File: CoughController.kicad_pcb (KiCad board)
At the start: 2 copper layers, 144 x 100 mm, 59 parts, among them J1 カフＳＷ１, J10 音声入力, J11 音声出力, J12 DI-2, J13 DO-2, J14 CD1/CD2, J15 CF/MD, J16 IN1/IN2, J17 IN3/IN4, J2 カフＳＷ２, J3 カフＳＷ３, J4 カフＳＷ４, J5 カフＳＷ５, J6 電源入力, J7 電源出力, J8 DI-1, J9 DO-1, K1 G6A-274P-ST-US DC12, K2 G6A-274P-ST-US DC12, U1 TLP627-2, U2 TLP627-2, U3 TLP627-2, U4 TLP627-2, U5 TLP627-2, U6 TLP627-2, U7 TLP627-2, U8 TLP627-2

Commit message: カフコントローラ
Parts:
- added J18: Out, Connector_PinHeader_2.54mm:PinHeader_1x02_P2.54mm_Vertical, F.Cu at (79.3, 55.0)
- added J19: In, Connector_PinHeader_2.54mm:PinHeader_1x03_P2.54mm_Vertical, F.Cu at (69.6, 55.0)
- J1: value カフＳＷ１ -> SW1; footprint Connector_PinHeader_1.27mm:PinHeader_1x04_P1.27mm_Vertical -> Connector_PinHeader_2.54mm:PinHeader_1x04_P2.54mm_Vertical
- J10: value 音声入力 -> AUDIO_IN; footprint Connector_PinHeader_1.27mm:PinHeader_1x06_P1.27mm_Vertical -> Connector_PinHeader_2.54mm:PinHeader_1x06_P2.54mm_Vertical
- J11: value 音声出力 -> AUDIO_OUT; footprint Connector_PinHeader_1.27mm:PinHeader_1x06_P1.27mm_Vertical -> Connector_PinHeader_2.54mm:PinHeader_1x06_P2.54mm_Vertical
- J14, J15, J16, J17: footprint Connector_PinHeader_1.27mm:PinHeader_1x09_P1.27mm_Vertical -> Connector_PinHeader_2.54mm:PinHeader_1x09_P2.54mm_Vertical
- J2: value カフＳＷ２ -> SW2; footprint Connector_PinHeader_1.27mm:PinHeader_1x04_P1.27mm_Vertical -> Connector_PinHeader_2.54mm:PinHeader_1x04_P2.54mm_Vertical
- J3: value カフＳＷ３ -> SW3; footprint Connector_PinHeader_1.27mm:PinHeader_1x04_P1.27mm_Vertical -> Connector_PinHeader_2.54mm:PinHeader_1x04_P2.54mm_Vertical
- J4: value カフＳＷ４ -> SW4; footprint Connector_PinHeader_1.27mm:PinHeader_1x04_P1.27mm_Vertical -> Connector_PinHeader_2.54mm:PinHeader_1x04_P2.54mm_Vertical
- J5: value カフＳＷ５ -> SW5; footprint Connector_PinHeader_1.27mm:PinHeader_1x04_P1.27mm_Vertical -> Connector_PinHeader_2.54mm:PinHeader_1x04_P2.54mm_Vertical
- J6: value 電源入力 -> PWR_IN
- J7: value 電源出力 -> PWR_OUT
- moved H3 183.4 mm to (55.0, 145.0)
- moved C2 104.5 mm to (93.0, 67.7)
- moved C1 104.3 mm to (93.0, 61.0)
- moved J6 104.0 mm to (90.5, 54.7)
- moved H2 103.5 mm to (183.0, 55.0)
- moved J16 97.1 mm to (144.7, 55.0), turned to -90 degrees
- moved H1 93.5 mm to (55.0, 55.0)
- moved J17 93.4 mm to (170.0, 55.0), turned to -90 degrees
- moved J5 88.3 mm to (69.4, 76.8), turned to 90 degrees
- moved J4 72.2 mm to (69.4, 91.8), turned to 90 degrees
- moved J7 66.5 mm to (108.0, 54.7)
- moved K2 58.7 mm to (112.8, 118.9), turned to 0 degrees
- moved J3 56.3 mm to (69.4, 106.8), turned to 90 degrees
- moved R4 53.3 mm to (105.2, 133.2)
- moved R5 51.4 mm to (115.5, 133.2)
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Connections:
- J12 pad 10: COM2 -> COM0
- J13 pad 10: COM2 -> COM0
- J13 pad 9: MCOM3 -> MCOM1
- J8 pad 1: unconnected-(J8-Pin_1-Pad1) -> Net-(J19-Pin_3)
- J8 pad 2: unconnected-(J8-Pin_2-Pad2) -> Net-(J19-Pin_2)
- J8 pad 3: unconnected-(J8-Pin_3-Pad3) -> Net-(J19-Pin_1)
- J9 pad 2: unconnected-(J9-Pin_2-Pad2) -> Net-(J18-Pin_2)
- J9 pad 3: unconnected-(J9-Pin_3-Pad3) -> Net-(J18-Pin_1)
- U1 pad 2: MCOM3 -> MCOM1
- U1 pad 4: MCOM3 -> MCOM1
- U2 pad 2: MCOM3 -> MCOM1
- U2 pad 4: MCOM3 -> MCOM1
- U3 pad 2: MCOM3 -> MCOM1
- U3 pad 4: MCOM3 -> MCOM1
- U4 pad 2: MCOM3 -> MCOM1
- U4 pad 4: MCOM3 -> MCOM1
- U5 pad 6: MCOM3 -> MCOM1
- U5 pad 8: MCOM3 -> MCOM1
- U6 pad 6: MCOM3 -> MCOM1
- U6 pad 8: MCOM3 -> MCOM1
- U7 pad 6: MCOM3 -> MCOM1
- U7 pad 8: MCOM3 -> MCOM1
- U8 pad 6: MCOM3 -> MCOM1
- U8 pad 8: MCOM3 -> MCOM1
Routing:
- net MCOM1: track 0.00 -> 402.8 mm
- net COM0: track 0.00 -> 277.4 mm
- net Net-(J13-Pin_8): track 0.00 -> 75.9 mm
- net Net-(J13-Pin_7): track 0.00 -> 66.8 mm
- net Net-(J18-Pin_1): track 0.00 -> 65.8 mm
- net RY_POW: track 0.00 -> 65.2 mm
- net Net-(J18-Pin_2): track 0.00 -> 63.5 mm
- net Net-(J1-Pin_2): track 0.00 -> 61.8 mm
- net Net-(J10-Pin_1): track 0.00 -> 60.5 mm
- net Net-(J2-Pin_2): track 0.00 -> 58.1 mm
- net Net-(J13-Pin_1): track 0.00 -> 58.1 mm
- net Net-(J13-Pin_6): track 0.00 -> 57.8 mm
- net Net-(J5-Pin_3): track 0.00 -> 55.5 mm
- net Net-(J13-Pin_5): track 0.00 -> 54.9 mm
- net Net-(J4-Pin_3): track 0.00 -> 45.9 mm
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- removed copper zone on B.Cu, net MCOM1
- removed copper zone on F.Cu, net MCOM1
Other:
- board size 144 x 100 mm -> 138 x 100 mm
- board text added: "AUDIO IN"
- board text added: "AUDIO OUT"
- board text added: "DI-1"
- board text added: "DI-1/6-7"
- board text added: "DI-1/6-8"
- board text added: "DI-2"
- board text added: "DI-2/1-4"
- board text added: "DI-2/5-8"
- board text added: "DO-1"
- board text added: "DO-2"
- board text added: "DO-2/1-4"
- board text added: "DO-2/5-8"
- board text added: "PWR IN"
- board text added: "PWR OUT"

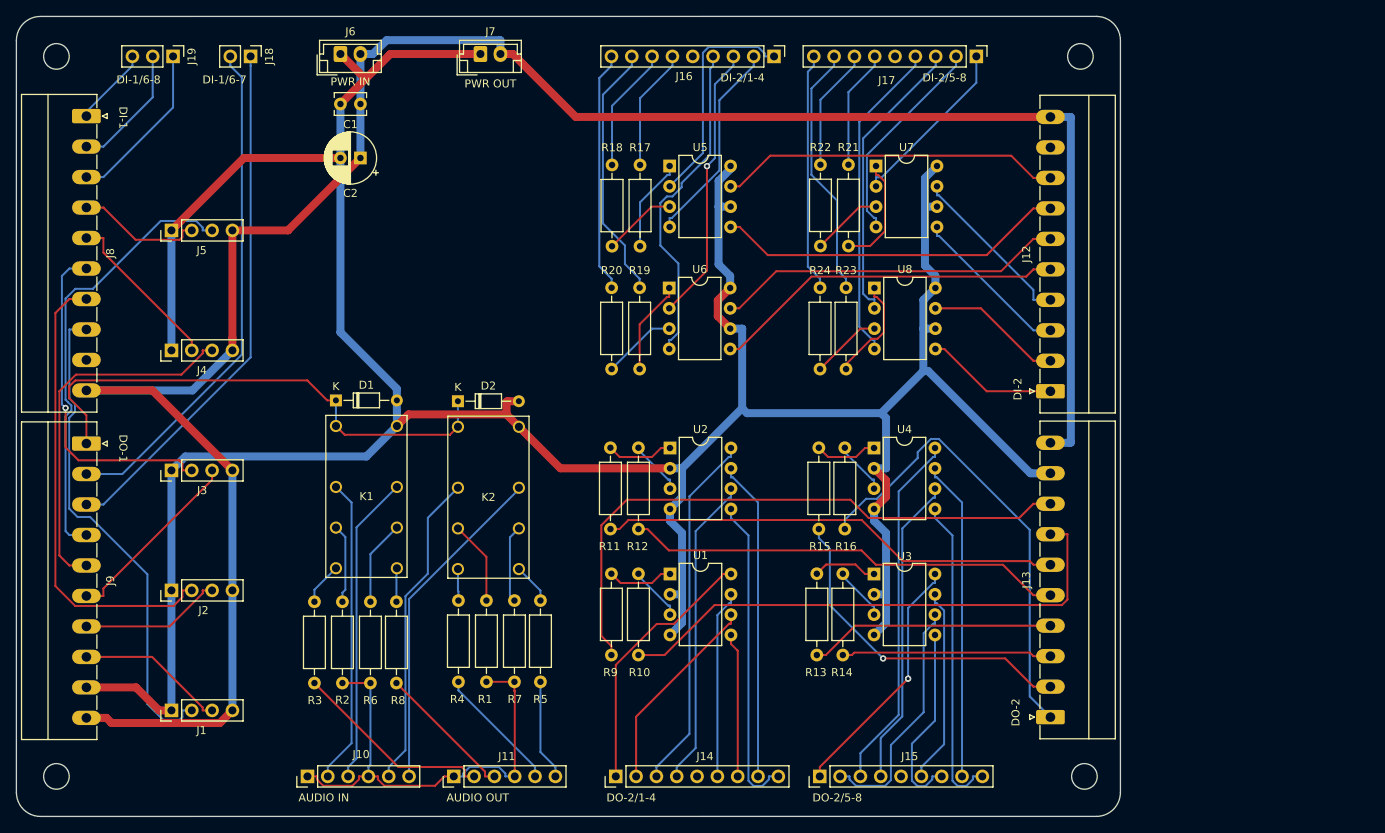
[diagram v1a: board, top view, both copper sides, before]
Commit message: コネクタをピンヘッダに変更
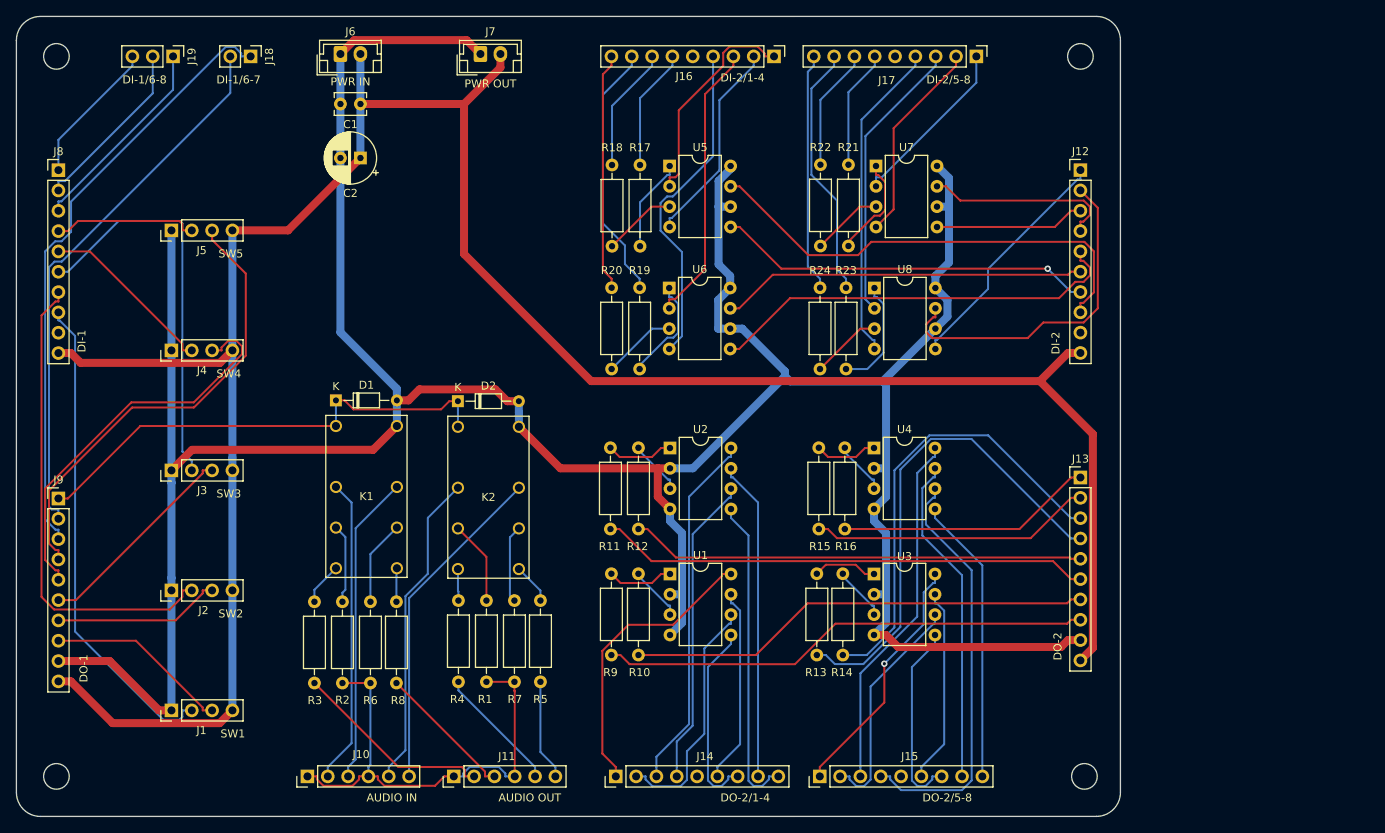
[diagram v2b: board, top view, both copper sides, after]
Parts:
- J12, J13, J8, J9: footprint Connector_Phoenix_MC:PhoenixContact_MC_1,5_10-G-3.81_1x10_P3.81mm_Horizontal -> Connector_PinHeader_2.54mm:PinHeader_1x10_P2.54mm_Vertical
- moved J13 30.2 mm to (183.0, 107.6), turned to 0 degrees
- moved J12 27.9 mm to (183.0, 69.2), turned to 0 degrees
- moved J9 7.71 mm to (55.2, 110.3), turned to 0 degrees
- moved J8 7.61 mm to (55.2, 69.2), turned to 0 degrees
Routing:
- net Net-(J13-Pin_4): track 30.7 -> 61.8 mm
- net Net-(J13-Pin_3): track 26.3 -> 56.9 mm
- net COM0: track 277.4 -> 303.4 mm
- net Net-(J13-Pin_1): track 58.1 -> 32.1 mm
- net Net-(J12-Pin_2): track 17.1 -> 42.6 mm
- net Net-(J12-Pin_8): track 42.7 -> 58.7 mm
- net Net-(J13-Pin_8): track 75.9 -> 61.4 mm
- net Net-(J12-Pin_1): track 16.6 -> 30.2 mm
- net Net-(J15-Pin_4): track 38.9 -> 52.2 mm
- net Net-(J18-Pin_1): track 65.8 -> 76.1 mm
- net Net-(J13-Pin_7): track 66.8 -> 58.1 mm
- net Net-(J12-Pin_5): track 44.2 -> 52.5 mm
- net Net-(J19-Pin_3): track 9.85 -> 18.1 mm
- net Net-(J3-Pin_2): track 42.5 -> 49.6 mm, vias 1 -> 0
- net Net-(J13-Pin_2): track 41.9 -> 35.3 mm, vias 1 -> 0
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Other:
- board text added: "SW1"
- board text added: "SW2"
- board text added: "SW3"
- board text added: "SW4"
- board text added: "SW5"
- board text added: "▲"

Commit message: 基板サイズ調整
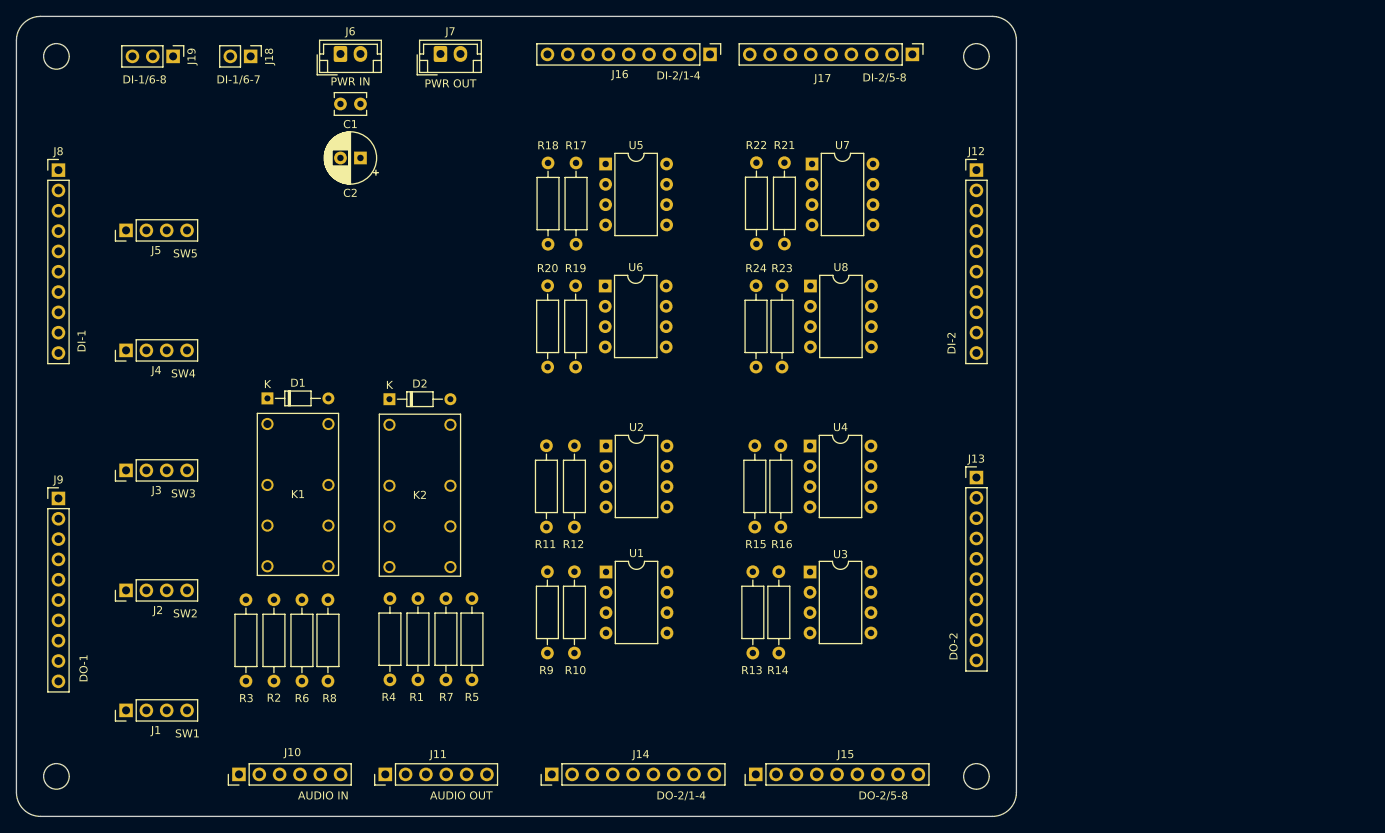
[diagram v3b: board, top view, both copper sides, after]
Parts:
- moved H4 13.5 mm to (170.0, 145.0)
- moved H2 13.0 mm to (170.0, 55.0)
- moved J12 13.0 mm to (170.0, 69.2)
- moved J13 13.0 mm to (170.0, 107.6)
- moved D1 8.56 mm to (81.4, 97.8)
- moved D2 8.56 mm to (96.6, 97.8)
- moved J10 8.56 mm to (77.8, 144.8)
- moved J11 8.56 mm to (96.1, 144.8)
- moved K1 8.56 mm to (89.0, 118.5)
- moved K2 8.56 mm to (104.2, 118.7)
- moved R1 8.56 mm to (100.2, 132.9)
- moved R2 8.56 mm to (82.2, 133.1)
- moved R3 8.56 mm to (78.7, 133.1)
- moved R4 8.56 mm to (96.7, 132.9)
- moved R5 8.56 mm to (106.9, 132.9)
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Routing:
- net MCOM1: track 404.1 -> 0.00 mm
- net COM0: track 303.4 -> 0.00 mm
- net Net-(J18-Pin_1): track 76.1 -> 0.00 mm
- net Net-(J18-Pin_2): track 68.7 -> 0.00 mm
- net Net-(J13-Pin_4): track 61.8 -> 0.00 mm
- net Net-(J13-Pin_8): track 61.4 -> 0.00 mm
- net Net-(J13-Pin_6): track 61.3 -> 0.00 mm
- net RY_POW: track 61.0 -> 0.00 mm
- net Net-(J1-Pin_2): track 61.0 -> 0.00 mm
- net Net-(J10-Pin_1): track 60.5 -> 0.00 mm
- net Net-(J2-Pin_2): track 60.1 -> 0.00 mm
- net Net-(J12-Pin_8): track 58.7 -> 0.00 mm
- net Net-(J5-Pin_3): track 58.3 -> 0.00 mm
- net Net-(J13-Pin_7): track 58.1 -> 0.00 mm
- net Net-(J13-Pin_3): track 56.9 -> 0.00 mm
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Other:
- board size 138 x 100 mm -> 125 x 100 mm

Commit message: ルーティング見直し
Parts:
- moved U5 30.3 mm to (101.0, 88.5), turned to 90 degrees
- moved R15 30.3 mm to (156.2, 130.6), turned to 90 degrees
- moved R17 28.1 mm to (93.8, 88.6)
- moved R16 27.9 mm to (152.8, 130.6), turned to 90 degrees
- moved U7 25.6 mm to (137.4, 91.0), turned to 90 degrees
- moved U4 24.9 mm to (149.8, 128.6), turned to 180 degrees
- moved R18 21.7 mm to (97.2, 88.6)
- moved J16 20.8 mm to (115.9, 54.8), turned to 90 degrees
- moved J17 20.8 mm to (141.2, 54.8), turned to 90 degrees
- moved R24 20.5 mm to (162.9, 92.8)
- moved R21 20.0 mm to (130.5, 91.1)
- moved R11 19.1 mm to (129.0, 117.8), turned to 90 degrees
- moved R12 19.1 mm to (132.5, 117.8), turned to 90 degrees
- moved R9 16.9 mm to (129.0, 130.6), turned to 90 degrees
- moved R10 16.8 mm to (132.2, 130.6), turned to 90 degrees
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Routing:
- net MCOM1: track 0.00 -> 358.2 mm
- net COM0: track 0.00 -> 282.2 mm
- net Net-(J12-Pin_8): track 0.00 -> 70.5 mm
- net Net-(J18-Pin_1): track 0.00 -> 70.5 mm
- net Net-(J18-Pin_2): track 0.00 -> 67.2 mm
- net Net-(J12-Pin_7): track 0.00 -> 64.1 mm
- net Net-(J1-Pin_2): track 0.00 -> 61.2 mm
- net Net-(J10-Pin_1): track 0.00 -> 60.6 mm
- net Net-(J12-Pin_6): track 0.00 -> 59.1 mm
- net Net-(J12-Pin_5): track 0.00 -> 55.1 mm
- net RY_POW: track 0.00 -> 52.4 mm
- net Net-(J2-Pin_2): track 0.00 -> 51.6 mm
- net Net-(J5-Pin_3): track 0.00 -> 50.1 mm
- net Net-(J13-Pin_8): track 0.00 -> 48.3 mm
- net Net-(J13-Pin_6): track 0.00 -> 46.2 mm
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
